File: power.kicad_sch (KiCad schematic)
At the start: 18 parts, among them CN2 1.25T-2AW, J1 USB_C_Receptacle_USB2.0_14P, U3 AP2112K-3.3TRG1, U4 MCP73831T-2ACI/OT, U6 MSK-12C02_SMD_SPDT_SWITCH

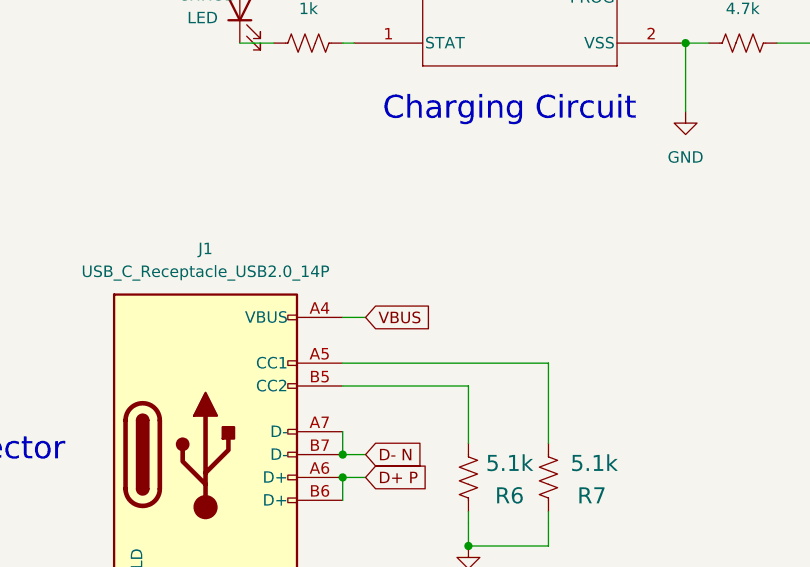
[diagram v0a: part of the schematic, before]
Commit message: Add NC points
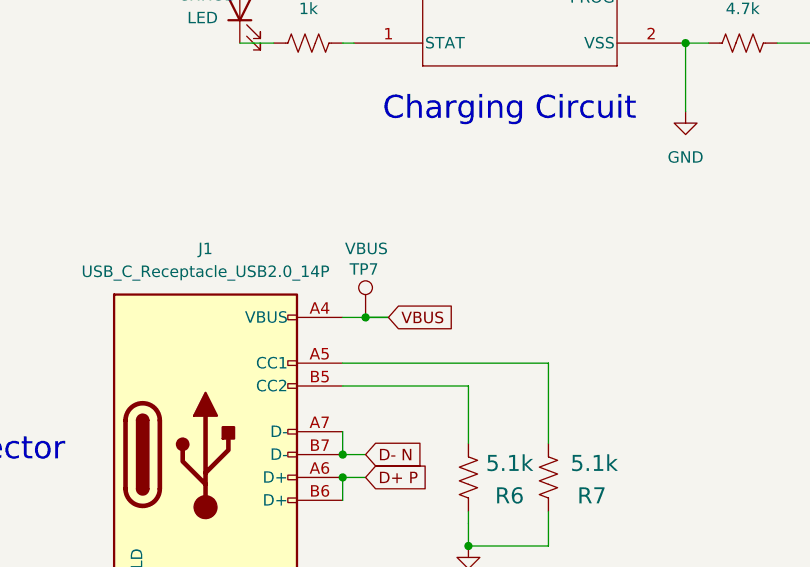
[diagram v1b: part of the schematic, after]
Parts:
- added TP7: VBUS, TestPoint:TestPoint_Pad_2.0x2.0mm, symbol uSlime:TestPoint
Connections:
- net VBUS: now also TP7.1
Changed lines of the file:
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@@
+	)
+	(junction
+		(at 166.37 118.11)
+		(diameter 0)
+		(color 0 0 0 0)
 	)
 	(junction
@@
 	(wire
 		(pts
+			(xy 168.91 118.11) (xy 166.37 118.11)
+		)
+		(stroke
+			(width 0)
+			(type default)
+		)
+	)
+	(wire
+		(pts
 			(xy 152.4 87.63) (xy 156.21 87.63)
 		)
@@
 			(width 0)
 			(type default)
+		)
+	)
+	(wire
+		(pts
+			(xy 166.37 118.11) (xy 168.91 118.11)
+		)
+		(stroke
+			(width 0.1524)
+			(type solid)
 		)
 	)
@@
 	(global_label "VBUS"
 		(shape input)
-		(at 166.37 118.11 0)
+		(at 168.91 118.11 0)
 		(fields_autoplaced yes)
 		(effects
@@
 		)
 		(property "Intersheetrefs" "${INTERSHEET_REFS}"
-			(at 174.2538 118.11 0)
+			(at 176.7938 118.11 0)
 			(effects
 				(font
@@
 					(unit 1)
 				)
+			)
+		)
+	)
+	(symbol
+		(lib_id "uSlime:TestPoint")
+		(at 166.37 118.11 0)
+		(unit 1)
+		(exclude_from_sim no)
+		(in_bom yes)
+		(on_board yes)
+		(dnp no)
+		(property "Reference" "TP7"
+			(at 164.592 112.776 0)
+			(effects
+				(font
+					(size 1.27 1.27)
+				)
+				(justify left)
+			)
+		)
+		(property "Value" "VBUS"
+			(at 164.084 110.49 0)
+			(effects
+				(font
+					(size 1.27 1.27)
+				)
+				(justify left)
+			)
+		)
+		(property "Footprint" "TestPoint:TestPoint_Pad_2.0x2.0mm"
+			(at 171.45 118.11 0)
+			(effects
+				(font
+					(size 1.27 1.27)
+				)
+				(hide yes)
+			)
+		)
+		(property "Datasheet" "~"
+			(at 171.45 118.11 0)
+			(effects
+				(font
+					(size 1.27 1.27)
+				)
+				(hide yes)
+			)
+		)
+		(property "Description" "test point"
+			(at 166.37 118.11 0)
+			(effects
+				(font
+					(size 1.27 1.27)
+				)
+				(hide yes)
+			)
+		)
+		(pin "1"
+		)
+		(instances
+			(project "uSlime"
+				(path "/f32c1c49-f803-4e7c-a530-6db148a7ba36/9141278c-15a6-43aa-8c9d-f1bdf7efadba"
+					(reference "TP7")
+					(unit 1)
+				)

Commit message: update power circuit
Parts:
- removed U6: MSK-12C02_SMD_SPDT_SWITCH, uSlime-libs:SW_PCM12SMTR, symbol uSlime:MSK-12C02_SMD_SPDT_SWITCH
- added C7: 10μF, Capacitor_SMD:C_0402_1005Metric, symbol uSlime:C
- added U2: MSK-12C02_SMD_SPDT_SWITCH, uSlime-libs:SW_PCM12SMTR, symbol uSlime:MSK-12C02_SMD_SPDT_SWITCH
- C5: value 10uF -> 10μF
- R5: value 4.7k -> 2k
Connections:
- net GND: now also C5.2, R5.2, C7.2, U2.GND; no longer C5.1, R5.1
- net VBAT: now also C5.1, U2.COM; no longer C5.2, CN2.1
- net VBUS: now also C7.1
- net at U4.5 (PROG): now also R5.1
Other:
- moved on the sheet: CHRG1, CN2, R3, R4, R5, U4

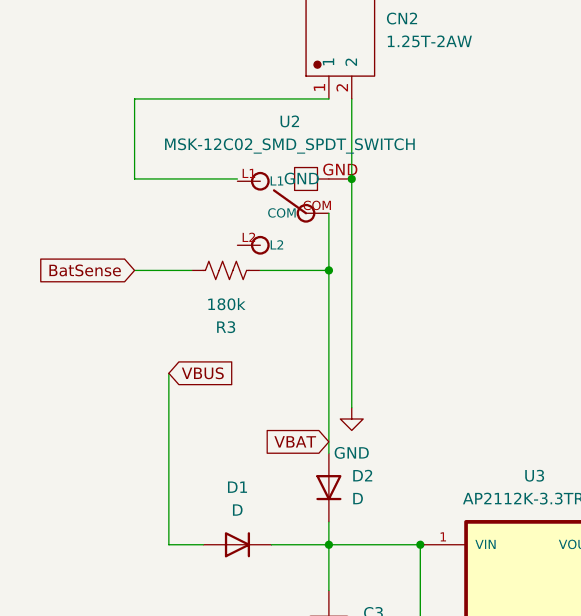
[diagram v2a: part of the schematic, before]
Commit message: Revamp pwr resistor, cap placement, fix switch sym
Fix placement of resistors and capacitor placement b/c additional
components were added to power circuit and weren't correct...

Also fixed switch symbol so wires actually connect to it in schematic
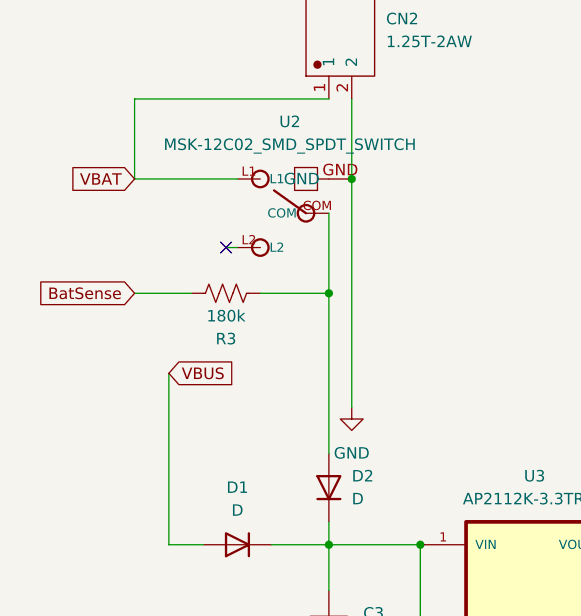
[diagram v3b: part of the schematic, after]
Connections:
- net VBAT: now also CN2.1, U2.L1; no longer D2.2 (A), R3.1, U2.COM
- new net: D2.2 (A), R3.1, U2.COM
- no-connect marks 0 -> 1
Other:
- moved on the sheet: R3
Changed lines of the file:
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@@
 	)
 	(junction
-		(at 67.31 46.99)
+		(at 67.31 49.53)
 		(diameter 0)
 		(color 0 0 0 0)
@@
 		(color 0 0 0 0)
 	)
+	(no_connect
+		(at 55.88 44.45)
+	)
 	(wire
 		(pts
@@
 	(wire
 		(pts
-			(xy 59.69 46.99) (xy 67.31 46.99)
+			(xy 59.69 49.53) (xy 67.31 49.53)
 		)
 		(stroke
@@
 	(wire
 		(pts
+			(xy 55.88 44.45) (xy 57.15 44.45)
+		)
+		(stroke
+			(width 0)
+			(type default)
+		)
+	)
+	(wire
+		(pts
 			(xy 67.31 77.47) (xy 67.31 82.55)
 		)
@@
 	(wire
 		(pts
-			(xy 67.31 40.64) (xy 67.31 46.99)
+			(xy 67.31 40.64) (xy 67.31 49.53)
 		)
 		(stroke
@@
 	(wire
 		(pts
-			(xy 67.31 46.99) (xy 67.31 67.31)
+			(xy 67.31 49.53) (xy 67.31 67.31)
 		)
 		(stroke
@@
 	(wire
 		(pts
-			(xy 52.07 46.99) (xy 45.72 46.99)
+			(xy 52.07 49.53) (xy 45.72 49.53)
 		)
 		(stroke
@@
 		)
 	)
-	(global_label "VBAT"
+	(global_label "BatSense"
 		(shape input)
-		(at 67.31 66.04 180)
+		(at 45.72 49.53 180)
 		(fields_autoplaced yes)
 		(effects
@@
 		)
 		(property "Intersheetrefs" "${INTERSHEET_REFS}"
-			(at 59.91 66.04 0)
+			(at 34.0263 49.53 0)
 			(effects
 				(font
@@
 		)
 	)
-	(global_label "BatSense"
+	(global_label "VBAT"
 		(shape input)
-		(at 45.72 46.99 180)
+		(at 45.72 36.83 180)
 		(fields_autoplaced yes)
 		(effects
@@
 		)
 		(property "Intersheetrefs" "${INTERSHEET_REFS}"
-			(at 34.0263 46.99 0)
+			(at 38.32 36.83 0)
 			(effects
 				(font
@@
 	(symbol
 		(lib_id "uSlime:R_US")
-		(at 55.88 46.99 270)
+		(at 55.88 49.53 270)
 		(unit 1)
 		(exclude_from_sim no)
@@
 		(on_board yes)
 		(dnp no)
-		(fields_autoplaced yes)
 		(property "Reference" "R3"
-			(at 55.88 53.34 90)
+			(at 55.88 54.61 90)
 			(effects
 				(font
@@
 		)
 		(property "Value" "180k"
-			(at 55.88 50.8 90)
+			(at 55.88 52.07 90)
 			(effects
 				(font
@@
 		)
 		(property "Footprint" "Resistor_SMD:R_0402_1005Metric"
-			(at 55.626 48.006 90)
+			(at 55.626 50.546 90)
 			(effects
 				(font
@@
 		)
 		(property "Datasheet" "~"
-			(at 55.88 46.99 0)
+			(at 55.88 49.53 0)
 			(effects
 				(font
@@
 		)
 		(property "Description" "Resistor, US symbol"
-			(at 55.88 46.99 0)
-			(effects
-				(font
+			(at 55.88 49.53 0)
+			(effects
+				(font
